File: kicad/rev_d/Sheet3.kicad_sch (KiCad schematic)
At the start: 98 parts, among them U1 74HCT1G04, X10 ST-214C, X14 AAFP/AC97 audio, X16 PLB1-4I, X17 PLB1-4I, X18 PLB1-4I, X20 PLB1-4I

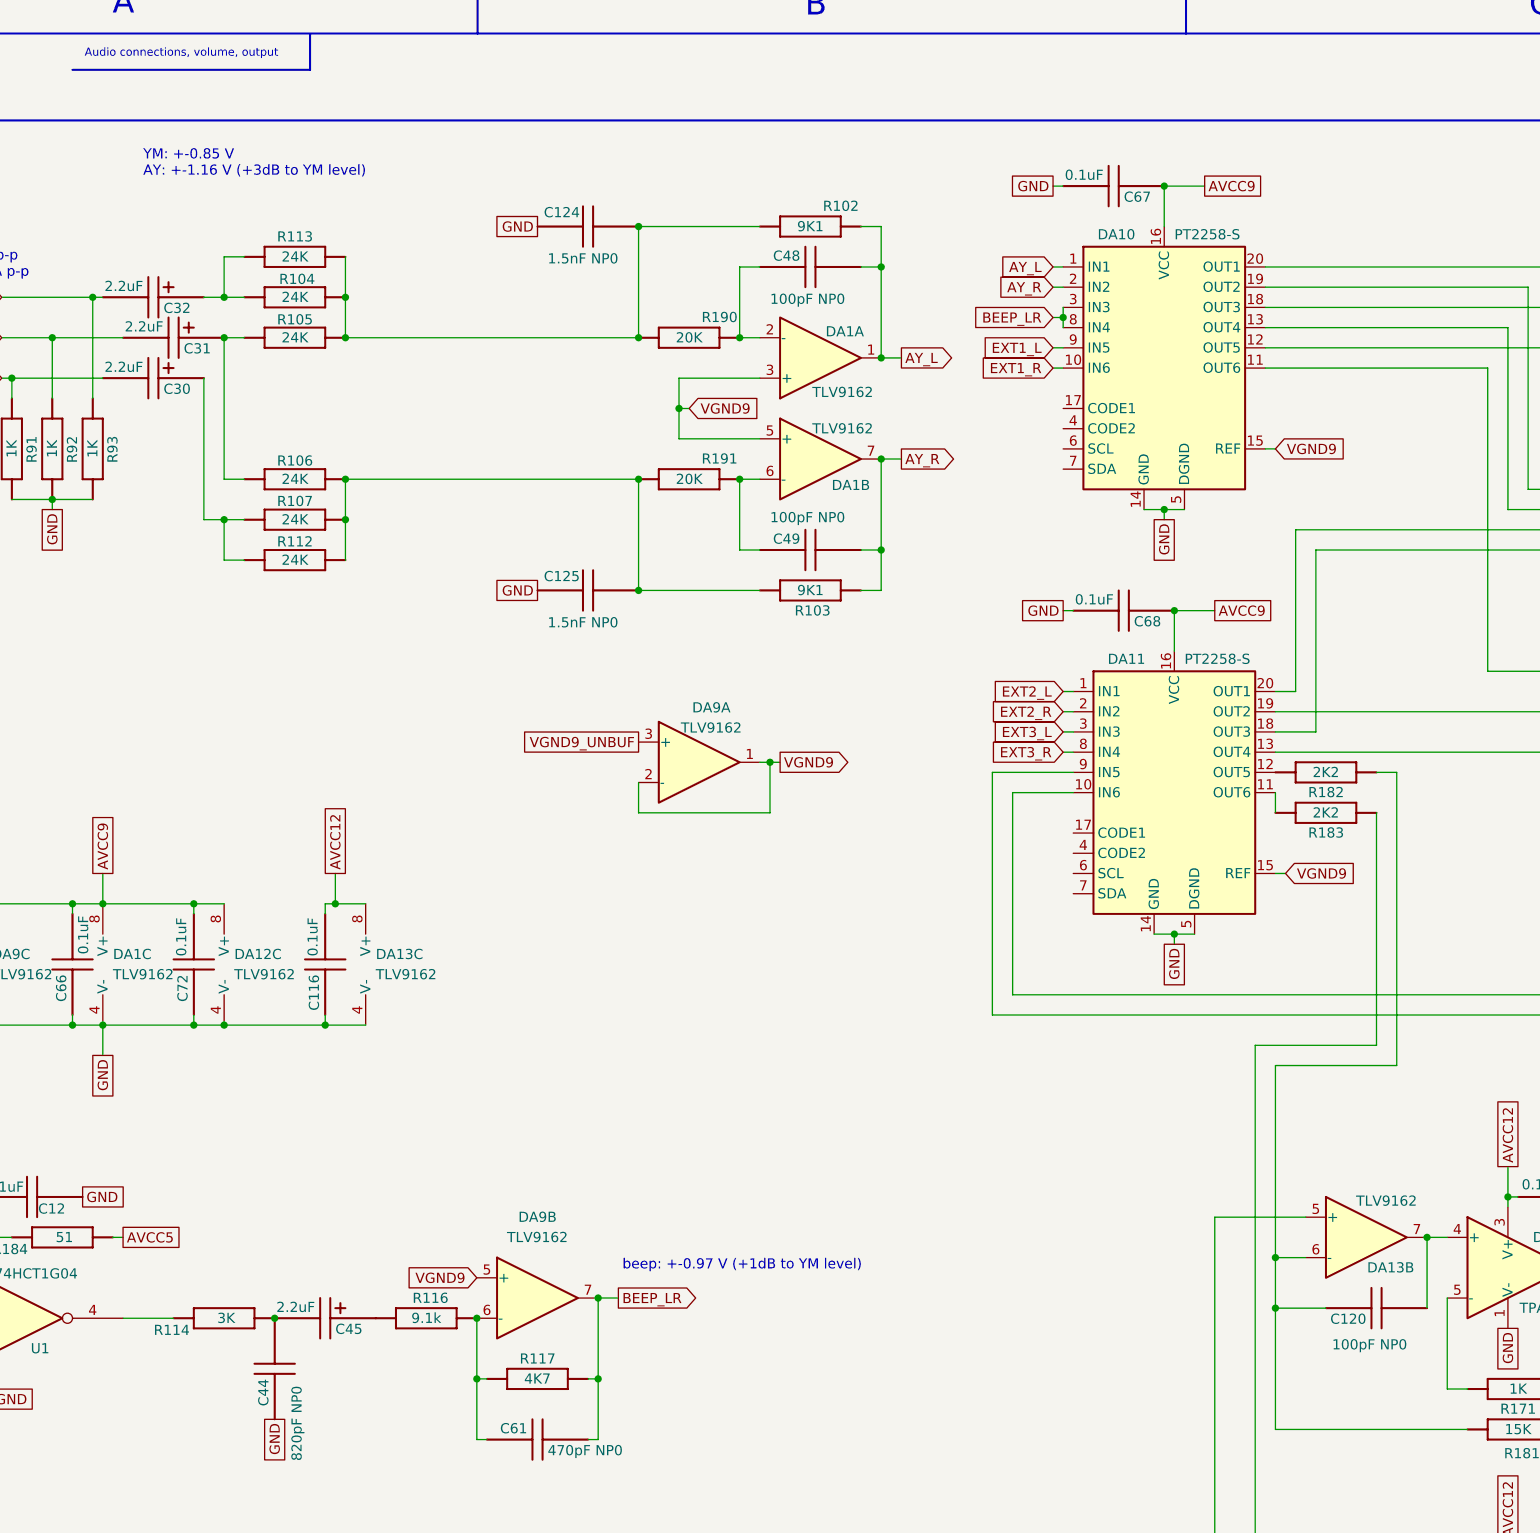
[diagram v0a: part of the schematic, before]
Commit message: pentevo: rev D: mfb_lowpass.py: add calculation of another lowpass for beeper
git-svn-id: svn://localhost/local-pentevo@1240 c6c76956-fad2-4150-a3a9-ea0a427205ba
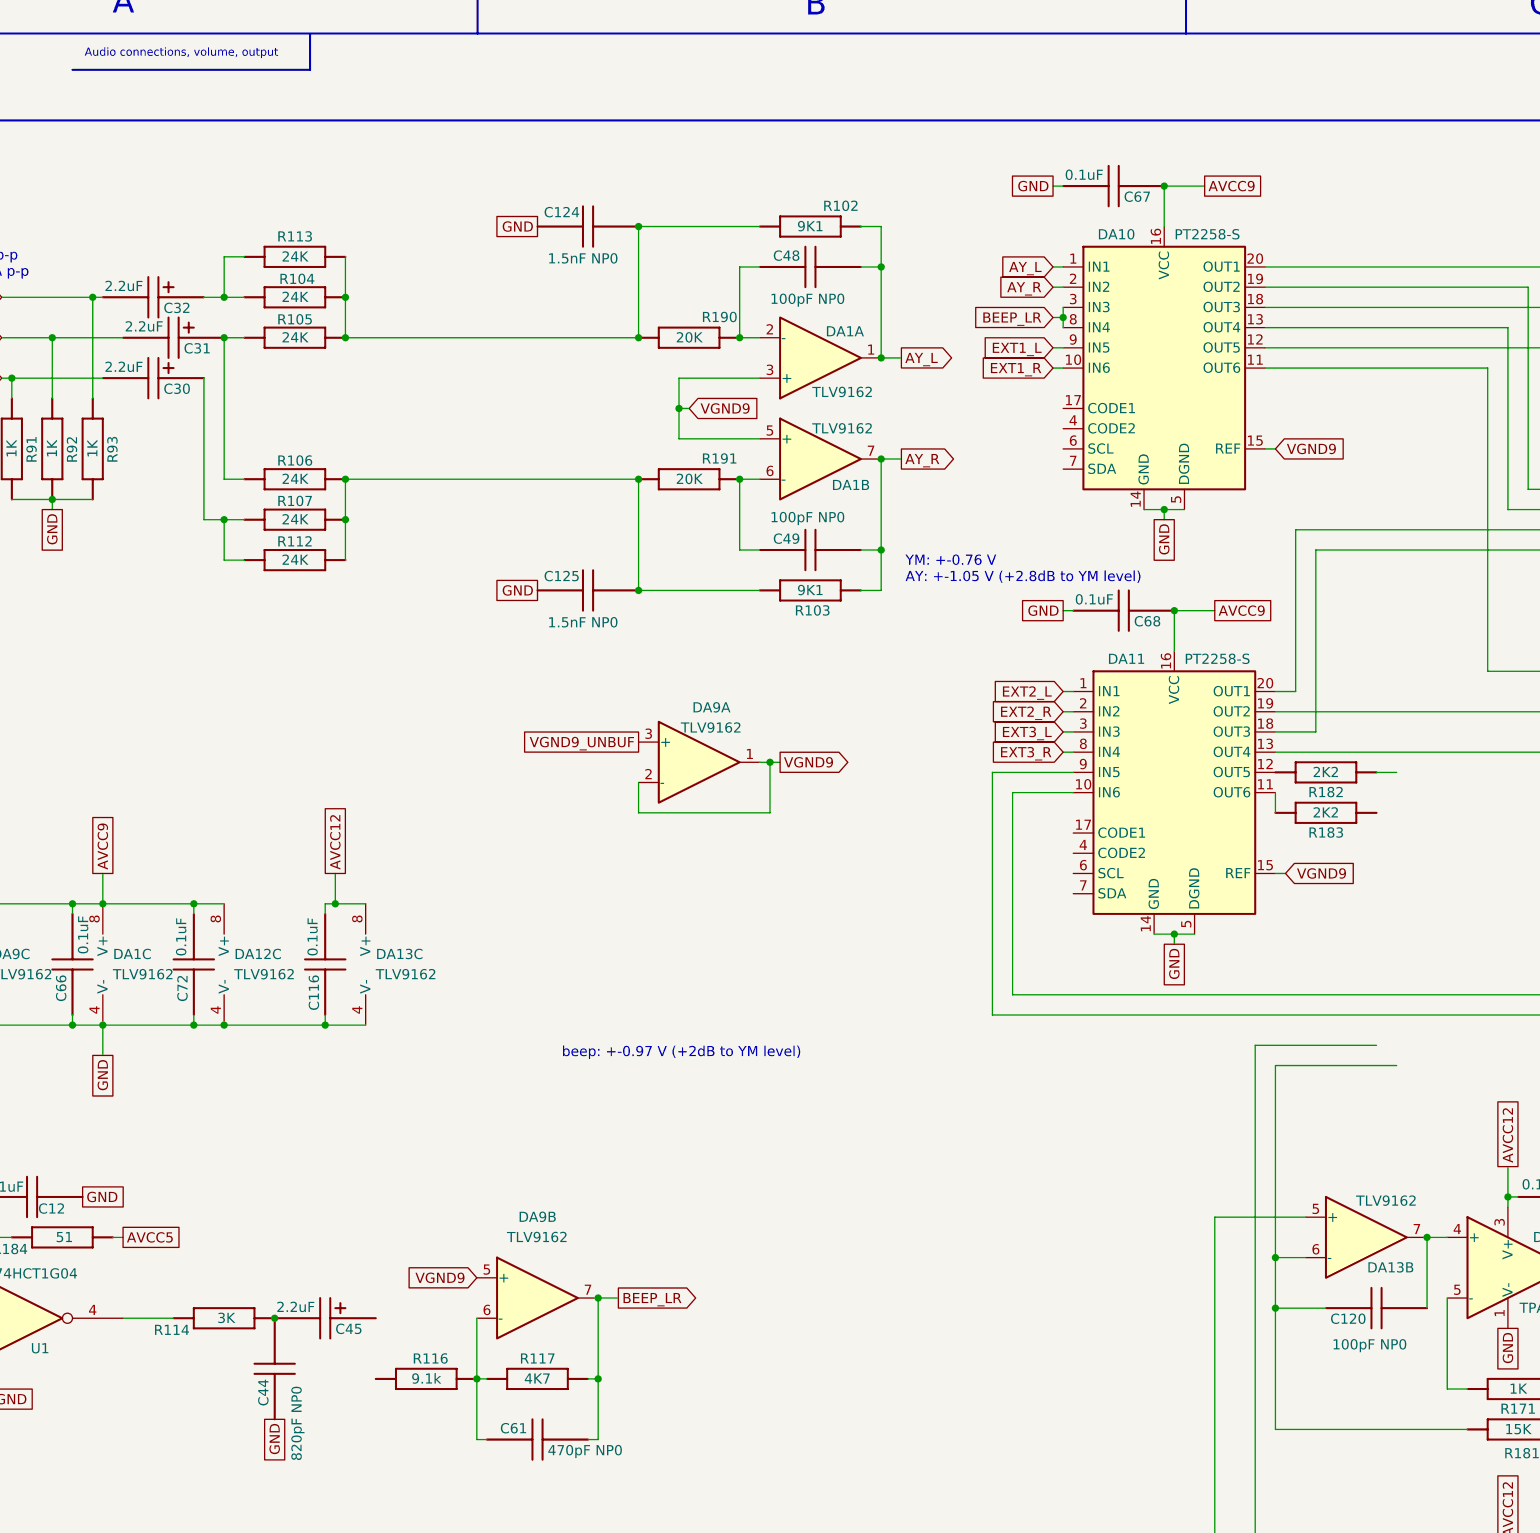
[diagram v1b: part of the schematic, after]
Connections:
- net at C121.1, DA13.2 (-), R180.1 (i/o): no longer R183.1 (i/o)
- net at R116.2 (i/o1): no longer C45.1
- net at C120.1, DA13.6 (-), R181.1 (i/o): no longer R182.1 (i/o)
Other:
- note added: "YM: +-0.76 V AY: +-1.05 V (+2.8dB to YM level)"
- note added: "beep: +-0.97 V (+2dB to YM level)"
- note removed: "YM: +-0.85 V AY: +-1.16 V (+3dB to YM level)"
- note removed: "beep: +-0.97 V (+1dB to YM level)"
- moved on the sheet: R116
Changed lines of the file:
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@@
 	)
 	(junction
-		(at 97.79 179.07)
-		(diameter 0)
-		(color 0 0 0 0)
-	)
-	(junction
 		(at 198.12 177.8)
 		(diameter 0)
@@
 	(wire
 		(pts
-			(xy 213.36 110.49) (xy 213.36 147.32)
-		)
-		(stroke
-			(width 0)
-			(type default)
-		)
-	)
-	(wire
-		(pts
 			(xy 234.95 57.15) (xy 234.95 62.23)
 		)
@@
 	(wire
 		(pts
+			(xy 97.79 186.69) (xy 97.79 179.07)
+		)
+		(stroke
+			(width 0)
+			(type default)
+		)
+	)
+	(wire
+		(pts
 			(xy 185.42 218.44) (xy 172.72 218.44)
 		)
@@
 	(wire
 		(pts
-			(xy 97.79 179.07) (xy 97.79 186.69)
-		)
-		(stroke
-			(width 0)
-			(type default)
-		)
-	)
-	(wire
-		(pts
 			(xy 170.18 46.99) (xy 171.45 46.99)
 		)
@@
 		)
 	)
-	(wire
-		(pts
-			(xy 210.82 115.57) (xy 210.82 144.78)
-		)
-		(stroke
-			(width 0)
-			(type default)
-		)
-	)
 	(polyline
 		(pts
@@
 		)
 	)
-	(text "beep: +-0.97 V (+1dB to YM level)"
+	(text "beep: +-0.97 V (+2dB to YM level)"
 		(exclude_from_sim no)
-		(at 116.078 172.466 0)
+		(at 108.458 145.796 0)
 		(effects
 			(font
@@
 		)
 	)
-	(text "YM: +-0.85 V\nAY: +-1.16 V (+3dB to YM level)"
+	(text "YM: +-0.76 V\nAY: +-1.05 V (+2.8dB to YM level)"
 		(exclude_from_sim no)
-		(at 55.88 34.036 0)
+		(at 151.638 85.09 0)
 		(effects
 			(font
@@
 	(symbol
 		(lib_id "eva-altium-import:Sheet2_0_RESCHIP")
-		(at 85.09 179.07 0)
+		(at 85.09 186.69 0)
 		(unit 1)
 		(exclude_from_sim no)
@@
 		(dnp no)
 		(property "Reference" "R116"
-			(at 94.234 177.292 0)
+			(at 94.234 184.912 0)
 			(effects
 				(font
@@
 		)
 		(property "Value" "9.1k"
-			(at 91.44 179.07 0)
+			(at 91.44 186.69 0)
 			(effects
 				(font
@@
 		)
 		(property "Footprint" "R-CHIP"
-			(at 85.09 179.07 0)
+			(at 85.09 186.69 0)
 			(effects
 				(font
@@
 		)
 		(property "Datasheet" ""
-			(at 85.09 179.07 0)
+			(at 85.09 186.69 0)
 			(effects
 				(font
@@
 		)
 		(property "Description" "RESCHIP"
-			(at 85.09 179.07 0)
+			(at 85.09 186.69 0)
 			(effects
 				(font
